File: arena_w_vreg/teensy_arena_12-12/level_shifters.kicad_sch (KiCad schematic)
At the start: 6 parts, among them U1 SPARKFUN_TXB0104, U2 SPARKFUN_TXB0104, U3 SPARKFUN_TXB0104, U4 SPARKFUN_TXB0104, U5 SPARKFUN_TXB0104, U6 SPARKFUN_TXB0104

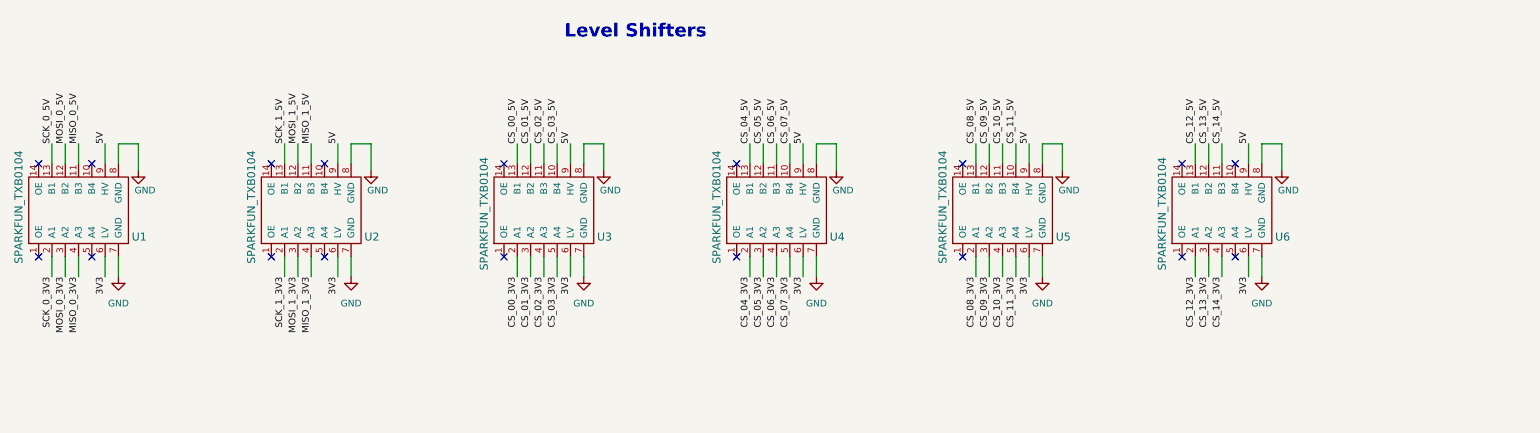
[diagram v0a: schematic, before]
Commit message: Worked on 12-12 teensy arena with voltage regulator.
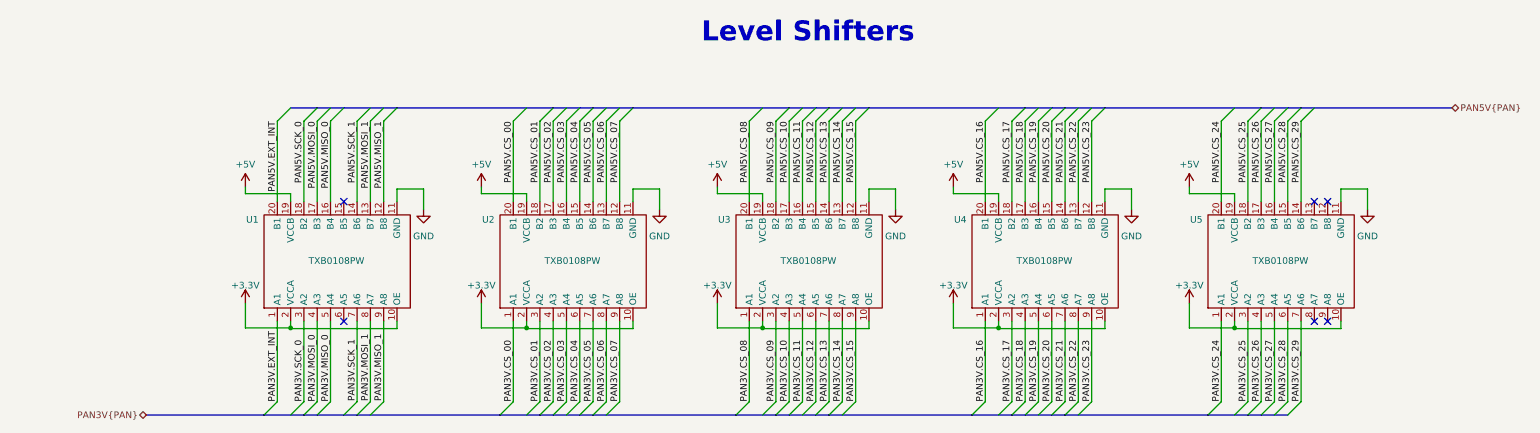
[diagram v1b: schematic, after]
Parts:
- removed U1, U2, U3, U4, U5, U6: SPARKFUN_TXB0104, arena_custom:SPARKFUN_TXB0104, symbol arena_custom:SPARKFUN_TXB0104
- added U1, U2, U3, U4, U5: TXB0108PW, symbol TXB0108:TXB0108PW
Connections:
- net GND: now also U1.11 (GND), U2.11 (GND), U3.11 (GND), U4.11 (GND), U5.11 (GND)
- new net +3.3V: U1.10 (OE), U1.2 (VCCA), U2.10 (OE), U2.2 (VCCA), U3.10 (OE), U3.2 (VCCA), U4.10 (OE), U4.2 (VCCA), U5.10 (OE), U5.2 (VCCA)
- new net +5V: U1.19 (VCCB), U2.19 (VCCB), U3.19 (VCCB), U4.19 (VCCB), U5.19 (VCCB)
- new net PAN3V.CS_00: U2.1 (A1)
- new net PAN3V.CS_01: U2.3 (A2)
- new net PAN3V.CS_02: U2.4 (A3)
- new net PAN3V.CS_03: U2.5 (A4)
- new net PAN3V.CS_04: U2.6 (A5)
- new net PAN3V.CS_05: U2.7 (A6)
- new net PAN3V.CS_06: U2.8 (A7)
- new net PAN3V.CS_07: U2.9 (A8)
- new net PAN3V.CS_08: U3.1 (A1)
- new net PAN3V.CS_09: U3.3 (A2)
- new net PAN3V.CS_10: U3.4 (A3)
- new net PAN3V.CS_11: U3.5 (A4)
- new net PAN3V.CS_12: U3.6 (A5)
- new net PAN3V.CS_13: U3.7 (A6)
- new net PAN3V.CS_14: U3.8 (A7)
- new net PAN3V.CS_15: U3.9 (A8)
- new net PAN3V.CS_16: U4.1 (A1)
- new net PAN3V.CS_17: U4.3 (A2)
- new net PAN3V.CS_18: U4.4 (A3)
- new net PAN3V.CS_19: U4.5 (A4)
- new net PAN3V.CS_20: U4.6 (A5)
- new net PAN3V.CS_21: U4.7 (A6)
- new net PAN3V.CS_22: U4.8 (A7)
- new net PAN3V.CS_23: U4.9 (A8)
- new net PAN3V.CS_24: U5.1 (A1)
- new net PAN3V.CS_25: U5.3 (A2)
- new net PAN3V.CS_26: U5.4 (A3)
- new net PAN3V.CS_27: U5.5 (A4)
- new net PAN3V.CS_28: U5.6 (A5)
- new net PAN3V.CS_29: U5.7 (A6)
- new net PAN3V.EXT_INT: U1.1 (A1)
- new net PAN3V.MISO_0: U1.5 (A4)
- new net PAN3V.MISO_1: U1.9 (A8)
- new net PAN3V.MOSI_0: U1.4 (A3)
- new net PAN3V.MOSI_1: U1.8 (A7)
- new net PAN3V.SCK_0: U1.3 (A2)
- new net PAN3V.SCK_1: U1.7 (A6)
- new net PAN5V.CS_00: U2.20 (B1)
- new net PAN5V.CS_01: U2.18 (B2)
- new net PAN5V.CS_02: U2.17 (B3)
- new net PAN5V.CS_03: U2.16 (B4)
- new net PAN5V.CS_04: U2.15 (B5)
- new net PAN5V.CS_05: U2.14 (B6)
- new net PAN5V.CS_06: U2.13 (B7)
- new net PAN5V.CS_07: U2.12 (B8)
- new net PAN5V.CS_08: U3.20 (B1)
- new net PAN5V.CS_09: U3.18 (B2)
- new net PAN5V.CS_10: U3.17 (B3)
- new net PAN5V.CS_11: U3.16 (B4)
- new net PAN5V.CS_12: U3.15 (B5)
- new net PAN5V.CS_13: U3.14 (B6)
- new net PAN5V.CS_14: U3.13 (B7)
- new net PAN5V.CS_15: U3.12 (B8)
- new net PAN5V.CS_16: U4.20 (B1)
- new net PAN5V.CS_17: U4.18 (B2)
- new net PAN5V.CS_18: U4.17 (B3)
- new net PAN5V.CS_19: U4.16 (B4)
- new net PAN5V.CS_20: U4.15 (B5)
- new net PAN5V.CS_21: U4.14 (B6)
- new net PAN5V.CS_22: U4.13 (B7)
- new net PAN5V.CS_23: U4.12 (B8)
- new net PAN5V.CS_24: U5.20 (B1)
- new net PAN5V.CS_25: U5.18 (B2)
- new net PAN5V.CS_26: U5.17 (B3)
- new net PAN5V.CS_27: U5.16 (B4)
- new net PAN5V.CS_28: U5.15 (B5)
- new net PAN5V.CS_29: U5.14 (B6)
- new net PAN5V.EXT_INT: U1.20 (B1)
- new net PAN5V.MISO_0: U1.16 (B4)
- new net PAN5V.MISO_1: U1.12 (B8)
- new net PAN5V.MOSI_0: U1.17 (B3)
- new net PAN5V.MOSI_1: U1.13 (B7)
- new net PAN5V.SCK_0: U1.18 (B2)
- new net PAN5V.SCK_1: U1.14 (B6)
- no-connect marks 18 -> 6

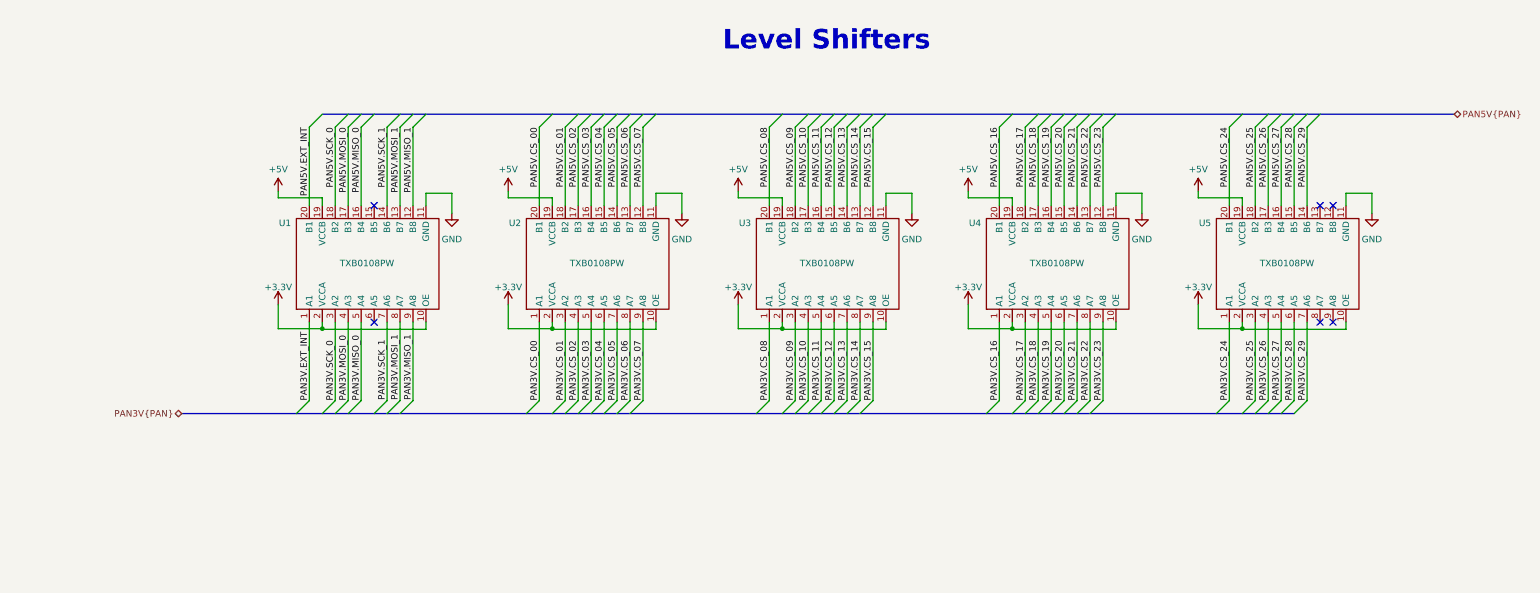
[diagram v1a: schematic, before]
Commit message: Worked on 12-12 teensy arean with voltage regulators.
Moved MOSFET to panel headers sheet. Added RESET to level sifters. Added
decouple caps for TXB0108's.
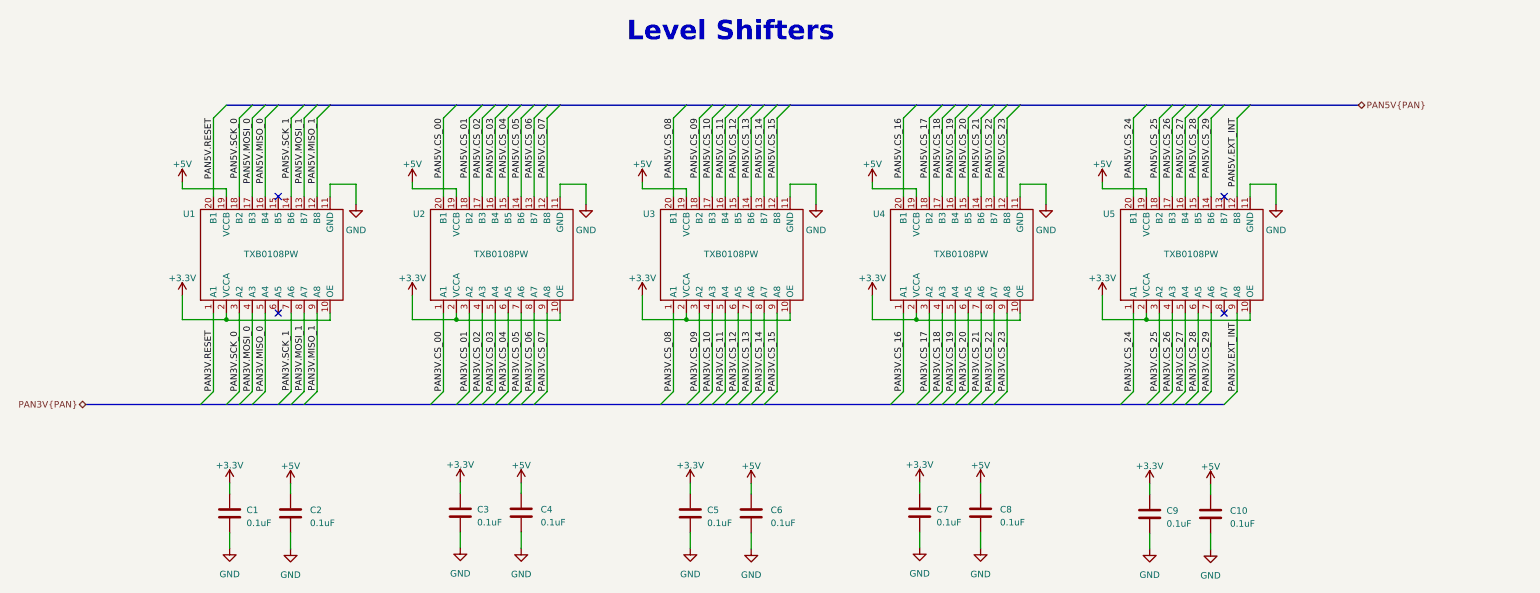
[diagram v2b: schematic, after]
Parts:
- added C1, C10, C2, C3, C4, C5, C6, C7, C8, C9: 0.1uF, symbol Device:C
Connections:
- net +3.3V: now also C1.1, C3.1, C5.1, C7.1, C9.1
- net +5V: now also C10.1, C2.1, C4.1, C6.1, C8.1
- net GND: now also C1.2, C10.2, C2.2, C3.2, C4.2, C5.2, C6.2, C7.2, C8.2, C9.2
- net PAN3V.EXT_INT: now also U5.9 (A8); no longer U1.1 (A1)
- net PAN5V.EXT_INT: now also U5.12 (B8); no longer U1.20 (B1)
- new net PAN3V.RESET: U1.1 (A1)
- new net PAN5V.RESET: U1.20 (B1)
- no-connect marks 6 -> 4
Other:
- moved on the sheet: U1, U2, U3, U4, U5

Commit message: Wored on teensy arena.
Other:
- note added: "Notes 1. Currently have 1A per column (12A total) Is this enough? 2. Powering levelshifters using 5V from teensy ..."
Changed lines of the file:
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@@
     (stroke (width 0) (type default))
+  )
+  (text "Notes\n\n1. Currently have 1A per column (12A total)\n   Is this enough?\n\n2. Powering levelshifters using 5V from teensy ... "
+    (at 287.909 73.787 0)
+    (effects (font (size 2.54 2.54)) (justify left bottom))
   )
   (text "Level Shifters" (at 139.954 23.114 0)

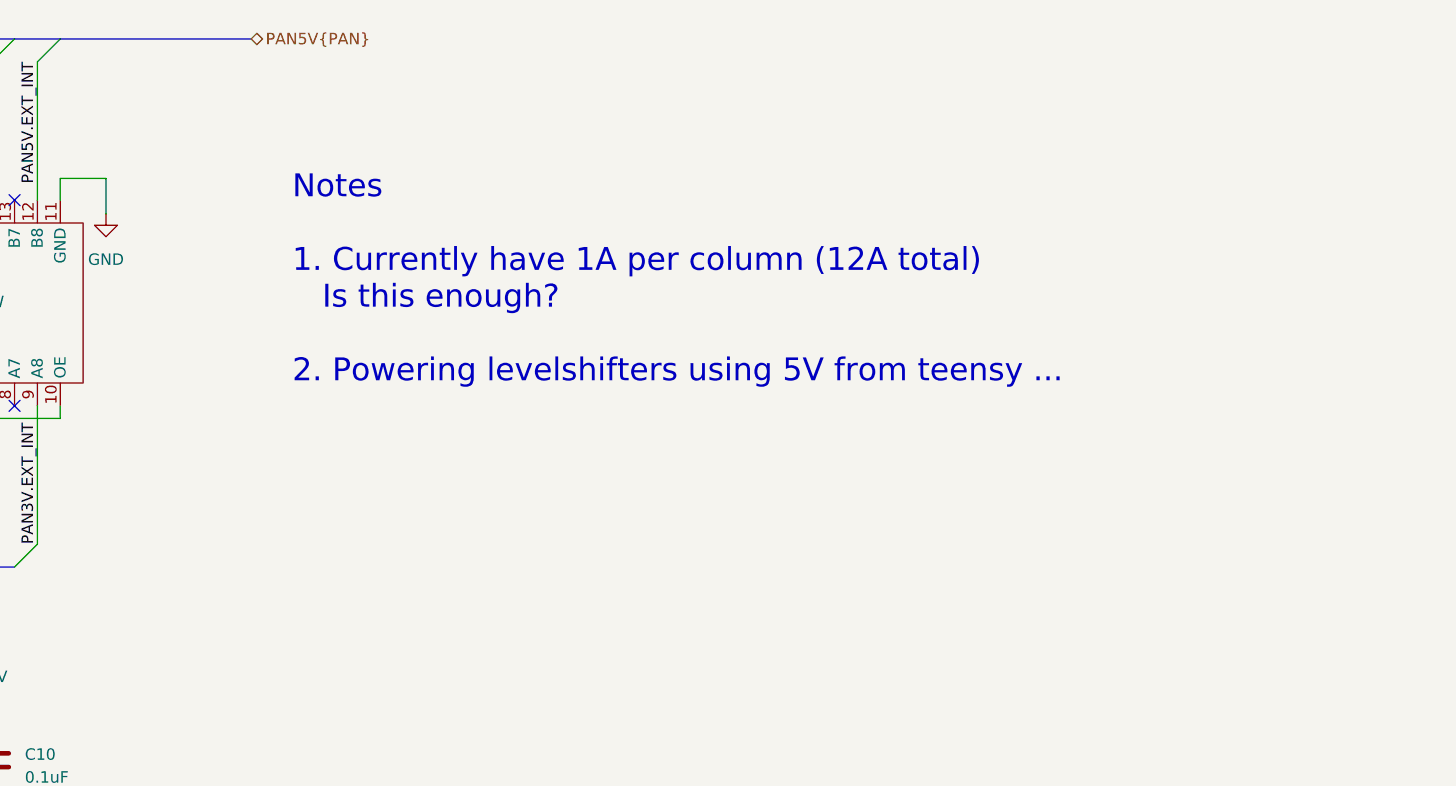
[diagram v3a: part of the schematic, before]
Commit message: Finished footprint assignment. Added notes. Modified header footprint.
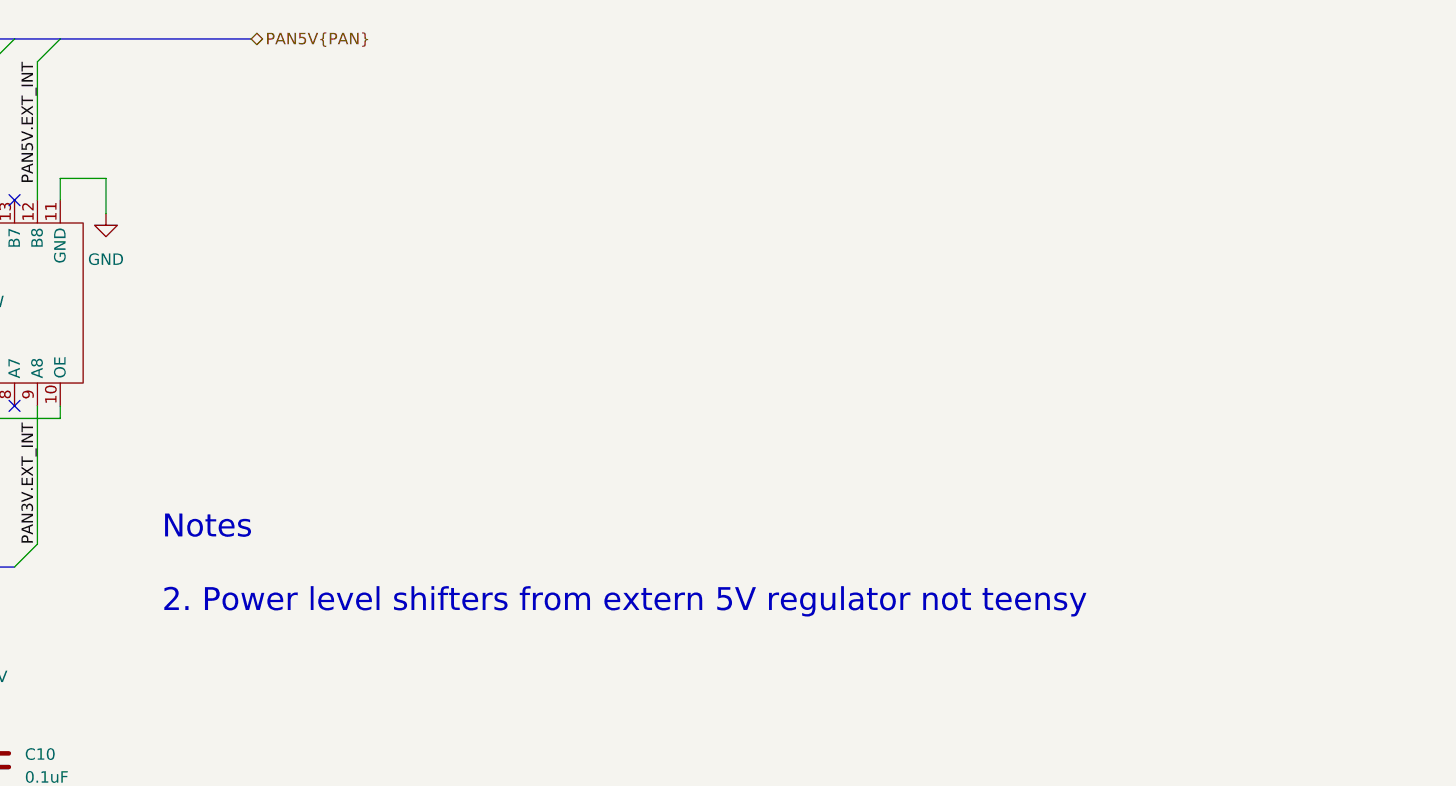
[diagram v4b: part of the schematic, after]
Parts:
- C1, C10, C2, C3, C4, C5, C6, C7, C8, C9: footprint (none) -> Capacitor_SMD:C_0603_1608Metric
- U1, U2, U3, U4, U5: footprint (none) -> Package_SO:TSSOP-20_4.4x6.5mm_P0.65mm
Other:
- note added: "Notes 2. Power level shifters from extern 5V regulator not teensy"
- note removed: "Notes 1. Currently have 1A per column (12A total) Is this enough? 2. Powering levelshifters using 5V from teensy ..."
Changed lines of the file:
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@@
     (stroke (width 0) (type default))
   )
-  (text "Notes\n\n1. Currently have 1A per column (12A total)\n   Is this enough?\n\n2. Powering levelshifters using 5V from teensy ... "
-    (at 287.909 73.787 0)
+  (text "Notes\n\n2. Power level shifters from extern 5V regulator not teensy\n"
+    (at 273.431 99.314 0)
     (effects (font (size 2.54 2.54)) (justify left bottom))
   )
@@
       (effects (font (size 1.27 1.27)) (justify left))
     )
-    (property "Footprint" "" (at 198.3232 118.999 0)
+    (property "Footprint" "Capacitor_SMD:C_0603_1608Metric" (at 198.3232 118.999 0)
       (effects (font (size 1.27 1.27)) hide)
     )
@@
       (effects (font (size 1.27 1.27)) (justify right))
     )
-    (property "Footprint" "" (at 52.578 39.243 0)
+    (property "Footprint" "Package_SO:TSSOP-20_4.4x6.5mm_P0.65mm" (at 52.578 39.243 0)
       (effects (font (size 1.27 1.27)) hide)
     )
@@
       (effects (font (size 1.27 1.27)) (justify left))
     )
-    (property "Footprint" "" (at 75.0062 119.126 0)
+    (property "Footprint" "Capacitor_SMD:C_0603_1608Metric" (at 75.0062 119.126 0)
       (effects (font (size 1.27 1.27)) hide)
     )
@@
       (effects (font (size 1.27 1.27)) (justify left))
     )
-    (property "Footprint" "" (at 255.3462 119.253 0)
+    (property "Footprint" "Capacitor_SMD:C_0603_1608Metric" (at 255.3462 119.253 0)
       (effects (font (size 1.27 1.27)) hide)
     )
@@
       (effects (font (size 1.27 1.27)) (justify left))
     )
-    (property "Footprint" "" (at 63.0682 119.126 0)
+    (property "Footprint" "Capacitor_SMD:C_0603_1608Metric" (at 63.0682 119.126 0)
       (effects (font (size 1.27 1.27)) hide)
     )
@@
       (effects (font (size 1.27 1.27)) (justify right))
     )
-    (property "Footprint" "" (at 232.918 39.243 0)
+    (property "Footprint" "Package_SO:TSSOP-20_4.4x6.5mm_P0.65mm" (at 232.918 39.243 0)
       (effects (font (size 1.27 1.27)) hide)
     )
@@
       (effects (font (size 1.27 1.27)) (justify left))
     )
-    (property "Footprint" "" (at 153.3652 119.126 0)
+    (property "Footprint" "Capacitor_SMD:C_0603_1608Metric" (at 153.3652 119.126 0)
       (effects (font (size 1.27 1.27)) hide)
     )
@@
       (effects (font (size 1.27 1.27)) (justify left))
     )
-    (property "Footprint" "" (at 108.2802 118.999 0)
+    (property "Footprint" "Capacitor_SMD:C_0603_1608Metric" (at 108.2802 118.999 0)
       (effects (font (size 1.27 1.27)) hide)
     )
@@
       (effects (font (size 1.27 1.27)) (justify left))
     )
-    (property "Footprint" "" (at 210.2612 118.999 0)
+    (property "Footprint" "Capacitor_SMD:C_0603_1608Metric" (at 210.2612 118.999 0)
       (effects (font (size 1.27 1.27)) hide)
     )
@@
       (effects (font (size 1.27 1.27)) (justify right))
     )
-    (property "Footprint" "" (at 97.663 39.243 0)
+    (property "Footprint" "Package_SO:TSSOP-20_4.4x6.5mm_P0.65mm" (at 97.663 39.243 0)
       (effects (font (size 1.27 1.27)) hide)
     )
@@
       (effects (font (size 1.27 1.27)) (justify left))
     )
-    (property "Footprint" "" (at 120.2182 118.999 0)
+    (property "Footprint" "Capacitor_SMD:C_0603_1608Metric" (at 120.2182 118.999 0)
       (effects (font (size 1.27 1.27)) hide)
     )
@@
       (effects (font (size 1.27 1.27)) (justify right))
     )
-    (property "Footprint" "" (at 142.748 39.243 0)
+    (property "Footprint" "Package_SO:TSSOP-20_4.4x6.5mm_P0.65mm" (at 142.748 39.243 0)
       (effects (font (size 1.27 1.27)) hide)
     )
@@
       (effects (font (size 1.27 1.27)) (justify left))
     )
-    (property "Footprint" "" (at 165.3032 119.126 0)
+    (property "Footprint" "Capacitor_SMD:C_0603_1608Metric" (at 165.3032 119.126 0)
       (effects (font (size 1.27 1.27)) hide)
     )
@@
       (effects (font (size 1.27 1.27)) (justify left))
     )
-    (property "Footprint" "" (at 243.4082 119.253 0)
+    (property "Footprint" "Capacitor_SMD:C_0603_1608Metric" (at 243.4082 119.253 0)
       (effects (font (size 1.27 1.27)) hide)
     )
@@
       (effects (font (size 1.27 1.27)) (justify right))
     )
-    (property "Footprint" "" (at 187.833 39.243 0)
-      (effects (font (size 1.27 1.27)) hide)
-    )
+    (property "Footprint" "Package_SO:TSSOP-20_4.4x6.5mm_P0.65mm" (at 187.833 39.243 0)
+      (effects (font (size 1.27 1.27)) hide)
+    )
